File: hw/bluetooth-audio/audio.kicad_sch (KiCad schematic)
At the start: 44 parts, among them J1 PJ-3537S-SMT, U3 TS5A23159DGS, U4 ES8388

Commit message: BOM sanity check: fix part numbers, populate passives, normalise fields
Full footprint + LCSC audit across power/audio/micro sheets (see
docs/bom-audit.md). Every part now carries Manufacturer + MPN + LCSC in one
consistent field set, validated against the jlcparts snapshot.

Corrections:
- Fix C1849 mis-assignment: it is a 10uF 1206 MLCC that had been pasted onto
  14 caps of unrelated values (incl. the 18pF crystal load caps); each
  reassigned to the correct part, stale Supplier Part Number cleared.
- D1 LED_BLUE was a white LED (C34499) -> C2293 (KT-0805B, blue).
- Populate all resistors/caps/L1 with JLCPCB parts (Basic where available;
  C0G for crystal-load 18pF, RF 3.3pF, and preserved on audio 100nF C41/C42).
- C48 SYS bulk MLCC -> 47uF/10V tantalum C22036 (DC-bias); footprint 3528-21.
- C27 10uF 0402 -> 0603 (match siblings). C19702.
- U3 footprint TSSOP-10 -> MSOP-10 (DGS = VSSOP, no thermal pad); C42751.
- Q2 -> C15127, J2 -> C5143397 (GCT USB-C), D6 LED_CHG -> amber C2296.
- J5 Molex -> JST-PH 3-pin battery connector S3B-PH-K-S (C157929).
- U9 (BQ24074 charger) marked DNP.
- Migrate all ICs/LEDs/discretes from Supplier Part Number to LCSC + add
  Manufacturer/MPN.

Adds docs/bom-audit.md with the priced BOM (~$11/board at 30 qty) and open
items (battery selection, U9 DNP, PCB re-sync).

Co-Authored-By: Claude Opus 4.8 <noreply@anthropic.com>
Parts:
- C1, C21: LCSC (none) -> C336270; MPN (none) -> EEEFT1E470AR; Manufacturer (none) -> PANASONIC
- C12, C13, C16, C18, C28, C30, C32, C43, C46: LCSC (none) -> C1525; MPN (none) -> CL05B104KO5NNNC; Manufacturer (none) -> Samsung Electro Mechanics
- C14, C15, C17, C29, C31, C44: LCSC (none) -> C19702; MPN (none) -> CL10A106KP8NNNC; Manufacturer (none) -> Samsung Electro Mechanics
- C24, C26: LCSC (none) -> C52923; MPN (none) -> CL05A105KA5NQNC; Manufacturer (none) -> Samsung Electro Mechanics
- C27: footprint Capacitor_SMD:C_0402_1005Metric -> Capacitor_SMD:C_0603_1608Metric; LCSC (none) -> C19702; MPN (none) -> CL10A106KP8NNNC; Manufacturer (none) -> Samsung Electro Mechanics
- C41, C42, C54: LCSC (none) -> C97946; MPN (none) -> GRM31C5C1H104JA01L; Manufacturer (none) -> Murata Electronics; Supplier Part Number C97946 -> (none)
- D7, D8: LCSC (none) -> C408389; MPN (none) -> BAT54S; Manufacturer (none) -> MDD Microdiode Semiconductor; Supplier Part Number C408389 -> (none)
- D7, D8: Supplier Part Number C408389 -> (none)
- R10, R16, R21, R7, R8, R9: LCSC (none) -> C25077; MPN (none) -> 0402WGF100JTCE; Manufacturer (none) -> UNI ROYAL Uniroyal Elec
- R19, R20: LCSC (none) -> C11702; MPN (none) -> 0402WGF1001TCE; Manufacturer (none) -> UNI ROYAL Uniroyal Elec
- R22, R23: LCSC (none) -> C25741; MPN (none) -> 0402WGF1003TCE; Manufacturer (none) -> UNI ROYAL Uniroyal Elec
- R27: LCSC (none) -> C25744; MPN (none) -> 0402WGF1002TCE; Manufacturer (none) -> UNI ROYAL Uniroyal Elec
- R41: LCSC (none) -> C17168; MPN (none) -> 0402WGF0000TCE; Manufacturer (none) -> UNI ROYAL Uniroyal Elec
- U3: footprint Package_SO:TSSOP-10_3x3mm_P0.5mm -> Package_SO:MSOP-10_3x3mm_P0.5mm; LCSC (none) -> C42751; MPN (none) -> TS5A23159DGSR; Manufacturer (none) -> Texas Instruments
- U4: LCSC (none) -> C365736; MPN (none) -> ES8388; Manufacturer (none) -> Everest Semiconductor; Supplier Part Number C365736 -> (none)

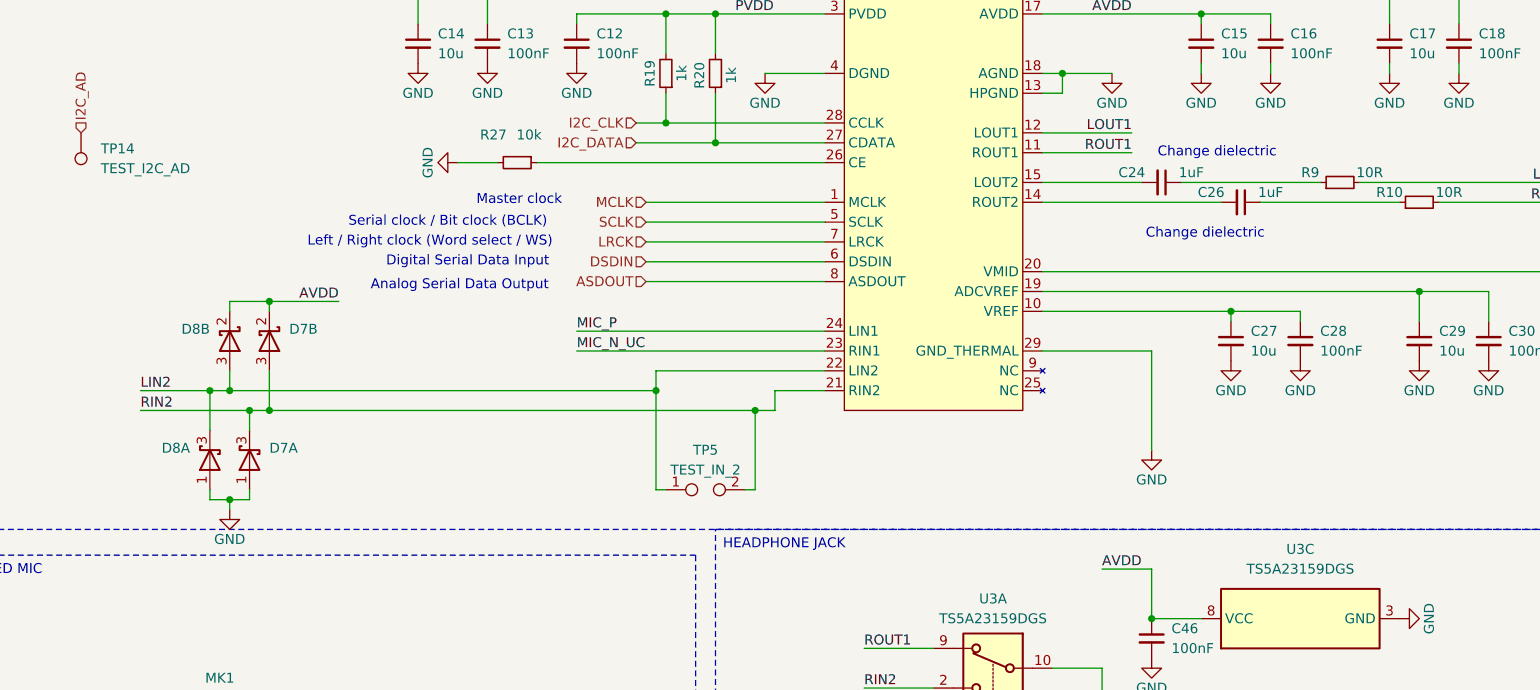
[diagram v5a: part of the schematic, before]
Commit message: Audio BOM: OUT2 couplers to electrolytic, C53 0402, C41/C42 land; place PCB
Schematic (audio + power sheets):
- C24/C26 (ES8388 OUT2 -> TP6 test-output couplers): 1uF MLCC -> 47uF
  electrolytic (Panasonic EEEFT1E470AR / C336270), matching C1/C21. Polarity
  verified against the netlist: + terminal to the codec/VMID side.
- C53 (USB_VBUS_SENSE divider filter): 1206 -> 0402 (house part
  CL05B104KO5NNNC / C1525).
- C41/C42 (mic C0G couplers): footprint aligned to plain C_1206_3216Metric,
  matching C54.

PCB: all footprints now placed in their initial positions, pending V1 routing.

Docs: design-overview.tex updated (delta #20 + 2026-09-16 revision entry). The
D7/D8 TX-input clamp removal is decided but recorded as pending -- that
schematic edit is being done by hand and is not in this commit.

Note: the deleted kicad-library submodule and the untracked in-project library
copies are deliberately left unstaged (broken/redundant state).

Co-Authored-By: Claude Opus 4.8 <noreply@anthropic.com>
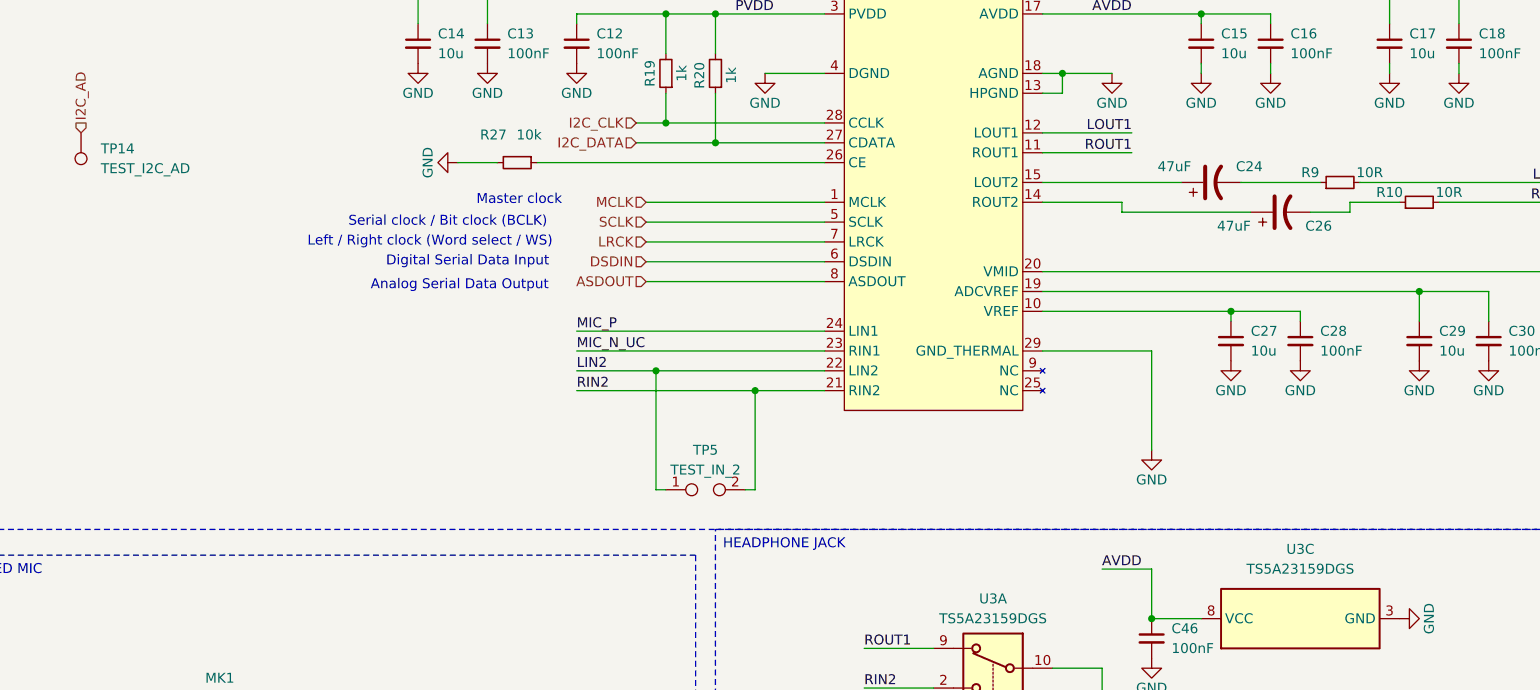
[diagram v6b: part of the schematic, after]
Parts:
- removed C24, C26: 1uF, Capacitor_SMD:C_0402_1005Metric, symbol Device:C_Small
- removed D7, D8: D_Schottky_Dual_Series_AKC_Split, Package_TO_SOT_SMD:SOT-23, symbol Device:D_Schottky_Dual_Series_AKC_Split
- added C24, C26: 47uF, Capacitor_SMD:CP_Elec_5x5.8, symbol Device:C_Polarized_US
- C41, C42, C54: footprint Capacitor_SMD:C_1206_3216Metric_Pad1.33x1.80mm_HandSolder -> Capacitor_SMD:C_1206_3216Metric
- U3: footprint Package_SO:TSSOP-10_3x3mm_P0.5mm -> Package_SO:MSOP-10_3x3mm_P0.5mm
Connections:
- net at R9.1: now also C24.2
- net at R10.1: now also C26.2
- net at U4.14 (ROUT2): now also C26.1
- net at U4.15 (LOUT2): now also C24.1
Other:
- note removed: "Change dielectric"
